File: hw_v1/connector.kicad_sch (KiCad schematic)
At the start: 1 part, among them J1 Conn_02x24_Counter_Clockwise

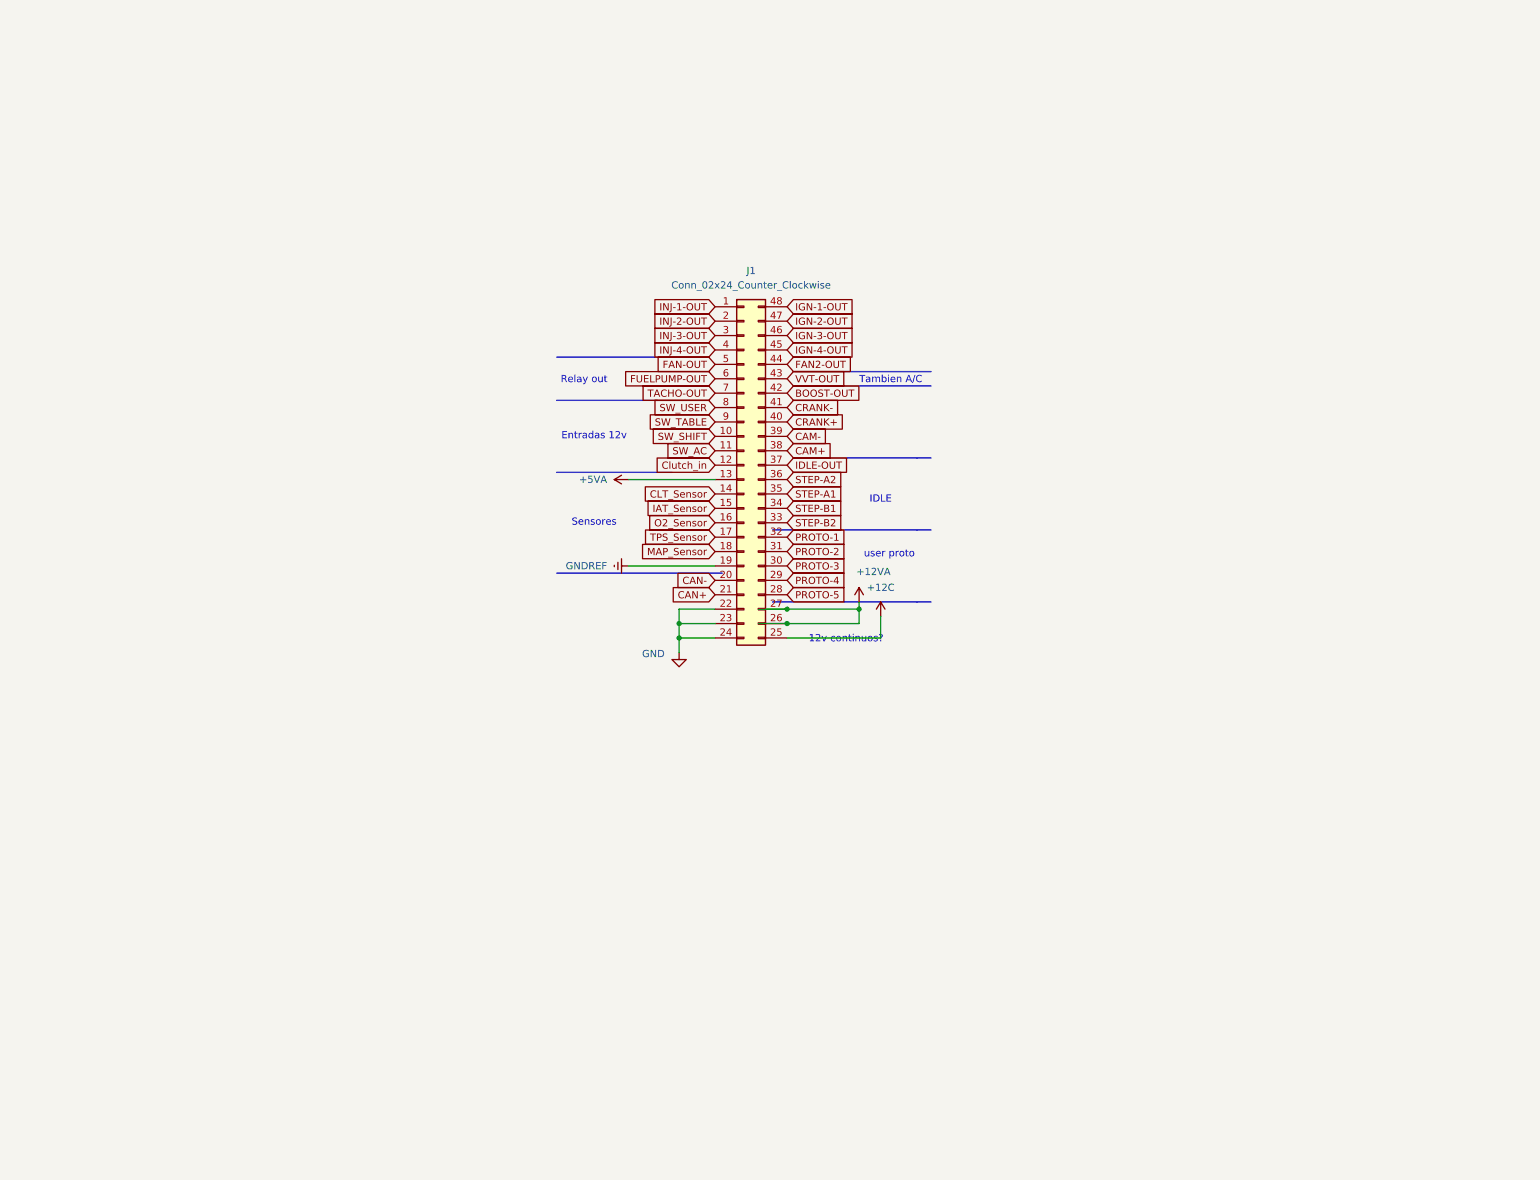
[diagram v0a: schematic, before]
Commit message: add sensors/ relay ouputs, connect all IO to mcu
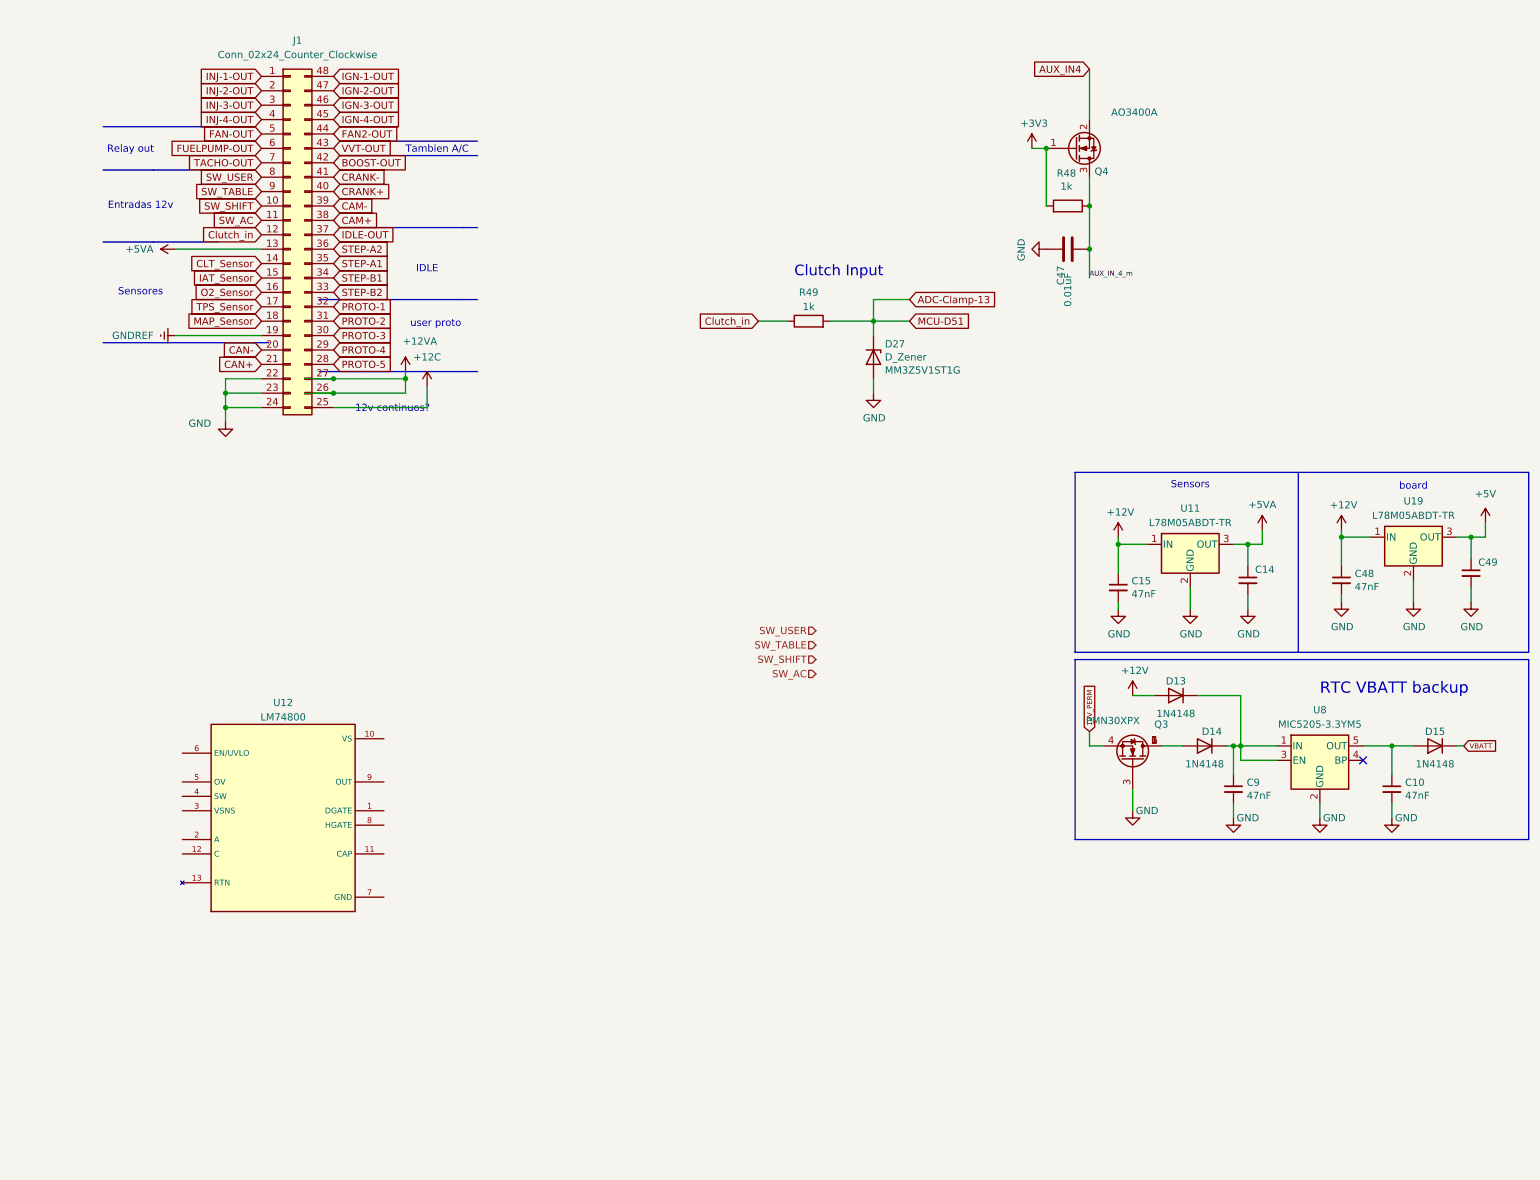
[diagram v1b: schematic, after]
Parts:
- added C10, C15, C48, C9: 47nF, Capacitor_SMD:C_0603_1608Metric, symbol Device:C_Small
- added C14, C49: 100nF, Capacitor_SMD:C_0805_2012Metric, symbol Device:C_Small
- added C47: 0.01uF, Capacitor_SMD:C_0805_2012Metric, symbol Device:C
- added D13, D14, D15: 1N4148, Diode_SMD:D_SOD-523, symbol Diode:1N4148
- added D27: D_Zener, Diode_SMD:D_SOD-323, symbol Device:D_Zener
- added Q3: PMN30XPX, Package_SO:TSOP-6_1.65x3.05mm_P0.95mm, symbol Transistor_FET:IRF540N
- added Q4: AO3400A, Package_TO_SOT_SMD:SOT-23, symbol Transistor_FET:AO3400A
- added R48: 1k, Resistor_SMD:R_0603_1608Metric, symbol Device:R
- added R49: 1k, Resistor_SMD:R_0805_2012Metric, symbol Device:R
- added U11, U19: L78M05ABDT-TR, Package_TO_SOT_SMD:TO-252-2, symbol Regulator_Linear:L7805
- added U12: LM74800, uEFI_v5:LM74800, symbol pdm_lib_v1:LM74800
- added U8: MIC5205-3.3YM5, Package_TO_SOT_SMD:SOT-23-5, symbol Regulator_Linear:MIC5205-3.3YM5
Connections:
- net +5VA: now also C14.1, U11.3 (OUT)
- net Clutch_in: now also R49.1
- net GND: now also C10.2, C14.2, C15.2, C47.1, C48.2, C49.2, C9.2, D27.2 (A), Q3.3 (G), U11.2 (GND), U19.2 (GND), U8.2 (GND)
- new net: D14.2 (A), Q3.1 (D), Q3.2 (D), Q3.5 (D), Q3.6 (D)
- new net: C9.1, D13.1 (K), D14.1 (K), U8.1 (IN), U8.3 (EN)
- new net: C10.1, D15.2 (A), U8.5 (OUT)
- new net +12V: C15.1, C48.1, D13.2 (A), U11.1 (IN), U19.1 (IN)
- new net +3V3: Q4.1 (G), R48.2
- new net +5V: C49.1, U19.3 (OUT)
- new net 12V_PERM: Q3.4 (S)
- new net ADC-Clamp-13: D27.1 (K), R49.2
- new net AUX_IN4: Q4.2 (S)
- new net AUX_IN_4_m: C47.2, Q4.3 (D), R48.1
- new net VBATT: D15.1 (K)
- no-connect marks 0 -> 1
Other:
- note added: "Clutch Input"
- note added: "RTC VBATT backup"
- note added: "Sensors"
- note added: "board"
- company: (none) -> Churrosoft ®
- title: (none) -> μEFI (Speeduino FW compatible)
- moved on the sheet: J1

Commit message: wip pcb layout
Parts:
- removed C10, C9: 47nF, Capacitor_SMD:C_0603_1608Metric, symbol Device:C_Small
- removed C47: 0.01uF, Capacitor_SMD:C_0805_2012Metric, symbol Device:C
- removed D13, D14, D15: 1N4148, Diode_SMD:D_SOD-523, symbol Diode:1N4148
- removed Q3: PMN30XPX, Package_SO:TSOP-6_1.65x3.05mm_P0.95mm, symbol Transistor_FET:IRF540N
- removed Q4: AO3400A, Package_TO_SOT_SMD:SOT-23, symbol Transistor_FET:AO3400A
- removed U8: MIC5205-3.3YM5, Package_TO_SOT_SMD:SOT-23-5, symbol Regulator_Linear:MIC5205-3.3YM5
- added C51, C52, C53: 0.1uF, Capacitor_SMD:C_0805_2012Metric, symbol Device:C_Small
- added C54: 10nF, Capacitor_SMD:C_0805_2012Metric, symbol Device:C_Small
- added C55: 100uF ±20% 35V, Capacitor_SMD:CP_Elec_6.3x7.7, symbol Device:CP_Small
- added D31, D32, D33, D34: 3.1v, Diode_SMD:D_SOD-323, symbol Device:D_Zener
- added D35: SM6T33A, Diode_SMD:D_SMB, symbol Diode:SM6T33A
- added J12: Delphi_Sicma_24, uEFI_v5:Delphi_Sicma_24_Grey, symbol Connector_Automotive:Delphi_Sicma_24
- added J13: Delphi_Sicma_24, uEFI_v5:Delphi_Sicma_24_Black, symbol Connector_Automotive:Delphi_Sicma_24
- added J14: Conn_01x04, Connector_PinHeader_2.54mm:PinHeader_1x04_P2.54mm_Vertical, symbol Connector_Generic:Conn_01x04
- added JP10, JP9: SolderJumper_3_Bridged12, Jumper:SolderJumper-3_P1.3mm_Bridged2Bar12_Pad1.0x1.5mm, symbol Jumper:SolderJumper_3_Bridged12
- added Q3: FDS6890A, Package_SO:SOP-8_3.9x4.9mm_P1.27mm, symbol Transistor_FET:FDS6890A
- added R59, R60, R61, R66: 1k, Resistor_SMD:R_0603_1608Metric, symbol Device:R
- added R62: 90k, Resistor_SMD:R_0603_1608Metric, symbol Device:R
- added R63: 900R, Resistor_SMD:R_0603_1608Metric, symbol Device:R
- added R64: 9.09k, Resistor_SMD:R_0603_1608Metric, symbol Device:R
- added R65: 3.48k, Resistor_SMD:R_0603_1608Metric, symbol Device:R
- added R67: 100R, Resistor_SMD:R_0603_1608Metric, symbol Device:R
- D27: value D_Zener -> 3.1v; Digikey Part Number MM3Z5V1ST1GOSCT-ND -> (none); LCSC (none) -> C5270765; Manufacturer_Name On Semi -> (none); Manufacturer_Part_Number MM3Z5V1ST1G -> (none); Part # MM3Z5V1ST1G -> BZT52C3V3S; URL https://www.digikey.com/product-detail/en/on-semiconductor/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 -> (none)
- R49: footprint Resistor_SMD:R_0805_2012Metric -> Resistor_SMD:R_0603_1608Metric; Digikey Part Number 311-1.00KCRCT-ND -> (none); LCSC (none) -> C21190; Manufacturer_Name Yageo -> (none); Manufacturer_Part_Number RC0805FR-071KL -> (none); URL https://www.digikey.com/product-detail/en/yageo/RC0805FR-07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 -> (none)
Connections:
- net +3V3 is gone; now on net Clutch_in: R48.2
- net AUX_IN_4_m is gone; now on net SW_Clutch_m: R48.1
- net +12V: now also U12.9 (OUT), C55.1, Q3.3 (S2)
- net +12VA: now also U12.2 (A), U12.3 (VSNS), C51.1, D35.1 (A1), J13.A1, Q3.1 (S1), R66.2
- net +5VA: now also J13.A3
- net BOOST-OUT: now also J12.C1
- net CLT_Sensor: now also J13.C5
- net Clutch_in: now also J13.B7; no longer R49.1
- net FAN-OUT: now also J12.C2
- net FUELPUMP-OUT: now also J12.C7
- net GND: now also U12.7 (GND), C51.2, C53.1, C54.1, C55.2, D31.2 (A), D32.2 (A), D33.2 (A), D34.2 (A), D35.2 (A2), J12.C8, J13.A2, J13.A8, J14.2 (Pin_2), R65.2
- net IAT_Sensor: now also J13.C6
- net IDLE-OUT: now also J12.C4
- net MAP_Sensor: now also J13.C8
- net O2_Sensor: now also J13.C4
- net SW_AC: now also R61.2
- net SW_SHIFT: now also R60.2
- net SW_TABLE: now also R59.2
- net SW_USER: now also R49.2
- net TACHO-OUT: now also J13.B1
- net TPS_Sensor: now also J13.C7
- net at U12.1 (DGATE): now also Q3.2 (G1)
- net at U12.10 (VS): now also U12.12 (C), C52.2
- net at U12.11 (CAP): now also C52.1
- net at U12.4 (SW): now also R63.1
- net at U12.5 (OV): now also R64.1, R65.1
- net at U12.6 (EN/UVLO): now also R66.1
- net at U12.8 (HGATE): now also Q3.4 (G2), R67.2
- net ADC-Clamp-13 renamed SW_Clutch_m
- net SW_Clutch_m: no longer R49.2
- net VVT-OUT renamed STEPPER-A1
- net STEPPER-A1: now also J12.C5
- new net: R62.1, R63.2
- new net: C54.2, R67.1
- new net: J14.4 (Pin_4), JP9.2 (C)
- new net: C53.2, Q3.5 (D2), Q3.6 (D2), Q3.7 (D1), Q3.8 (D1)
- new net: J14.3 (Pin_3), JP10.2 (C)
- new net CAM-IN+: J13.B4
- new net CAM-IN-: J13.B5
- new net CAN_H: J13.A7
- new net CAN_L: J13.A6
- new net CRANK-IN+: J13.B2
- new net CRANK-IN-: J13.B3
- new net Flex_Sensor: J13.B8
- new net GNDA: J13.C1
- new net IGN1: J12.B1
- new net IGN2: J12.B2
- new net IGN3: J12.B3
- new net IGN4: J12.B4
- new net IGN5: J12.B5
- new net IGN6: J12.B6
- new net IGN7: J12.B7
- new net IGN8: J12.B8
- new net INJ1: J12.A1
- new net INJ2: J12.A2
- new net INJ3: J12.A3
- new net INJ4: J12.A4
- new net INJ5: J12.A5
- new net INJ6: J12.A6
- new net INJ7: J12.A7
- new net INJ8: J12.A8
- new net SPARE1-Digital: J13.B6
- new net SPARE1-OUT: J12.C6
- new net SPARE1_Sensor: J13.C2
- new net SPARE2-Digital: J13.A5
- new net SPARE2-OUT: J12.C3
- new net SPARE2_Sensor: J13.C3
- new net SW_AC_m: D34.1 (K), R61.1
- new net SW_SHIFT_m: D33.1 (K), R60.1
- new net SW_TABLE_m: D32.1 (K), R59.1
- new net SW_USER_m: D31.1 (K), R49.1
- new net USART_2_RX: JP10.1 (A), JP9.3 (B)
- new net USART_2_TX: JP10.3 (B), JP9.1 (A)
- new net VBATT_MON: R62.2, R64.2
- new net VDD: J14.1 (Pin_1)
- no-connect marks 1 -> 0
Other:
- note added: "BLACK"
- note added: "Digital Inputs"
- note added: "GREY"
- note added: "HC-05 Bluetooth Connector"
- note added: "Revisar valores R66"
- note removed: "Clutch Input"
- note removed: "RTC VBATT backup"
- moved on the sheet: D27, J1, R48, U12
